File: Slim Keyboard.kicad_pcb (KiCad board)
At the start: 2 copper layers, 26 x 44 mm, 58 parts, among them J1 USB_C_Receptacle_USB2.0_16P, J2 SWD, J3 SWC, J5 S2B-PH-SM4-TB, U1 NRF52840-QIAA-R, U2 BQ24075RGT, U3 XC6220B331MR, Y1 ECS-.327-9-34B-TR, Y2 XRCGB32M000F1S2KR0

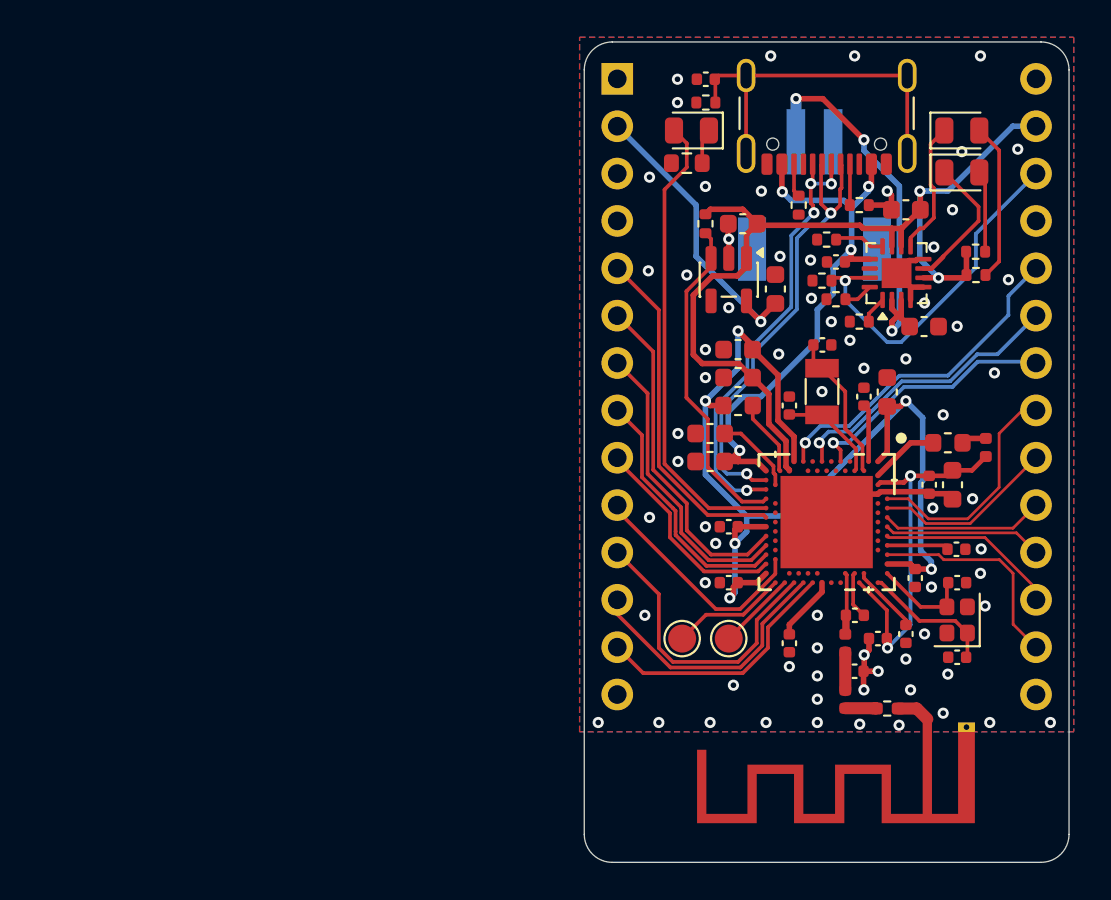
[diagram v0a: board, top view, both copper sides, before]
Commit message: DFM problems to solve; CE compliance issue
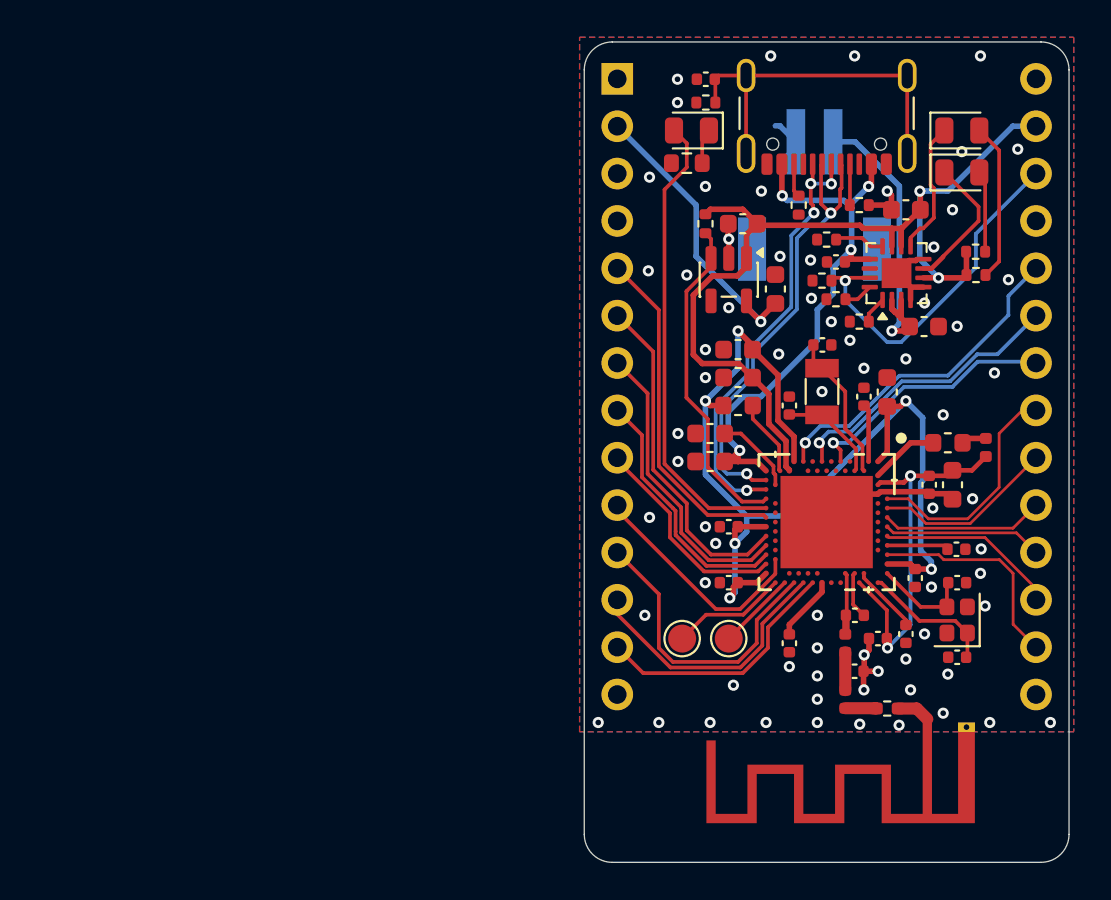
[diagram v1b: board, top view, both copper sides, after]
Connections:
- J5 pad 1: GND -> VBAT
- J5 pad 2: VBAT -> GND
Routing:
- net VBAT: track 21.9 -> 16.9 mm, vias 3 -> 1
- net GND: track 22.1 -> 25.1 mm
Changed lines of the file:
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@@
 		)
 		(pad "1" smd rect
-			(at 14.65 1.97 180)
+			(at 14.15 2.47 180)
 			(size 0.5 3.94)
 			(layers "F.Cu")
@@
 			(size 1 3.5)
 			(layers "B.Cu" "B.Mask" "B.Paste")
-			(net 1 "GND")
+			(net 17 "VBAT")
 			(pinfunction "1")
 			(pintype "passive")
@@
 			(size 1 3.5)
 			(layers "B.Cu" "B.Mask" "B.Paste")
-			(net 17 "VBAT")
+			(net 1 "GND")
 			(pinfunction "2")
 			(pintype "passive")
@@
 	)
 	(segment
+		(start 81.35 45.65)
+		(end 80.5 46.5)
+		(width 0.3)
+		(layer "B.Cu")
+		(net 1)
+	)
+	(segment
+		(start 80.492716 44.5)
+		(end 80.25 44.5)
+		(width 0.3)
+		(layer "B.Cu")
+		(net 1)
+	)
+	(segment
+		(start 81.35 45.357284)
+		(end 81.35 45.65)
+		(width 0.3)
+		(layer "B.Cu")
+		(net 1)
+	)
+	(segment
+		(start 81.35 45.357284)
+		(end 80.492716 44.5)
+		(width 0.3)
+		(layer "B.Cu")
+		(net 1)
+	)
+	(segment
+		(start 81.357742 45.349542)
+		(end 81.35 45.357284)
+		(width 0.6)
+		(layer "B.Cu")
+		(net 1)
+	)
+	(segment
 		(start 79.025 56.5)
 		(end 79.025 56.275)
@@
 	)
 	(segment
-		(start 84 73.73)
-		(end 84.02 73.75)
-		(width 0.2)
-		(layer "F.Cu")
-		(net 13)
-	)
-	(segment
-		(start 84 73.77)
-		(end 84.02 73.75)
-		(width 0.2)
-		(layer "F.Cu")
-		(net 13)
-	)
-	(segment
 		(start 81 71.77)
 		(end 81 71.25)
@@
 	)
 	(segment
-		(start 80.6 46.555)
-		(end 80.6 48.011026)
-		(width 0.3)
-		(layer "F.Cu")
-		(net 15)
-	)
-	(segment
-		(start 80.6 48.011026)
-		(end 80.623263 48.034289)
-		(width 0.3)
-		(layer "F.Cu")
-		(net 15)
-	)
-	(segment
 		(start 84.307625 51.145593)
 		(end 84.307625 51.592375)
@@
 	)
 	(segment
+		(start 80.6 48.226737)
+		(end 80.623263 48.25)
+		(width 0.3)
+		(layer "F.Cu")
+		(net 15)
+	)
+	(segment
 		(start 79.75 63)
 		(end 79.25 62.5)
@@
 	)
 	(segment
+		(start 80.6 46.555)
+		(end 80.6 48.226737)
+		(width 0.3)
+		(layer "F.Cu")
+		(net 15)
+	)
+	(segment
 		(start 79.25 62.5)
 		(end 78.25 62.5)
@@
 	)
 	(via
-		(at 80.623263 48.034289)
+		(at 80.623263 48.25)
 		(size 0.6)
 		(drill 0.3)
@@
 	)
 	(segment
+		(start 84.2149 48.7851)
+		(end 83.9298 48.5)
+		(width 0.3)
+		(layer "B.Cu")
+		(net 15)
+	)
+	(segment
 		(start 84.3399 50.897834)
 		(end 84.3399 48.9101)
@@
 	)
 	(segment
-		(start 81.088974 48.5)
-		(end 80.623263 48.034289)
+		(start 85.25 47.75)
+		(end 84.2149 48.7851)
 		(width 0.3)
 		(layer "B.Cu")
@@
 	)
 	(segment
-		(start 83.9298 48.5)
-		(end 81.088974 48.5)
-		(width 0.3)
-		(layer "B.Cu")
-		(net 15)
-	)
-	(segment
 		(start 82.5 54.355947)
 		(end 83.349 53.506947)
@@
 	)
 	(segment
-		(start 85.25 48)
-		(end 84.3399 48.9101)
+		(start 83.9298 48.5)
+		(end 80.873263 48.5)
 		(width 0.3)
 		(layer "B.Cu")
@@
 	)
 	(segment
-		(start 84.3399 48.9101)
-		(end 83.9298 48.5)
+		(start 77.721971 61.288621)
+		(end 77.721971 59.828324)
 		(width 0.3)
 		(layer "B.Cu")
@@
 	)
 	(segment
-		(start 85.25 47.75)
-		(end 85.25 48)
+		(start 84.3399 48.9101)
+		(end 84.2149 48.7851)
 		(width 0.3)
 		(layer "B.Cu")
@@
 	)
 	(segment
-		(start 77.721971 61.288621)
-		(end 77.721971 59.828324)
+		(start 77.721971 59.828324)
+		(end 78.525148 59.025147)
 		(width 0.3)
 		(layer "B.Cu")
@@
 	)
 	(segment
-		(start 77.721971 59.828324)
-		(end 78.525148 59.025147)
+		(start 80.873263 48.5)
+		(end 80.623263 48.25)
 		(width 0.3)
 		(layer "B.Cu")
@@
 	)
 	(segment
-		(start 85 45.25)
-		(end 82.793096 43.043096)
+		(start 87 54.5)
+		(end 87 54.814411)
 		(width 0.3)
 		(layer "F.Cu")
@@
 	)
 	(segment
-		(start 82.793096 43.043096)
-		(end 81.357742 43.043096)
+		(start 86.5 55.5)
+		(end 87.214411 55.5)
 		(width 0.3)
 		(layer "F.Cu")
@@
 	)
 	(segment
-		(start 86.5 55.5)
-		(end 86.5 55)
+		(start 87.214411 55.5)
+		(end 87.45 55.264411)
 		(width 0.3)
 		(layer "F.Cu")
@@
 	)
 	(segment
+		(start 87 54.5)
+		(end 86.685589 54.5)
+		(width 0.3)
+		(layer "F.Cu")
+		(net 17)
+	)
+	(segment
 		(start 87 53.8375)
-		(end 87 54.814411)
+		(end 87 54.5)
 		(width 0.3)
 		(layer "F.Cu")
@@
 	)
 	(segment
-		(start 86.5 55)
-		(end 86.842795 54.657205)
+		(start 86.685589 54.5)
+		(end 86.5 54.314411)
 		(width 0.3)
 		(layer "F.Cu")
@@
 	)
 	(via
-		(at 85 45.25)
-		(size 0.6)
-		(drill 0.3)
-		(layers "F.Cu" "B.Cu")
-		(free yes)
-		(net 17)
-	)
-	(via
 		(at 86.5 55.5)
 		(size 0.6)
@@
 		(net 17)
 	)
-	(via
-		(at 81.357742 43.043096)
-		(size 0.6)
-		(drill 0.3)
-		(layers "F.Cu" "B.Cu")
-		(free yes)
-		(net 17)
-	)
-	(segment
-		(start 81.357742 43.043096)
-		(end 81.357742 45.349542)
-		(width 0.6)
-		(layer "B.Cu")
-		(net 17)
-	)
 	(segment
 		(start 86.901 47.730346)
-		(end 85 45.829346)
-		(width 0.3)
-		(layer "B.Cu")
-		(net 17)
-	)
-	(segment
-		(start 85 45.829346)
-		(end 85 45.25)
+		(end 84.527938 45.357284)
 		(width 0.3)
 		(layer "B.Cu")
@@
 	)
 	(segment
-		(start 81.35 43.050838)
-		(end 81.357742 43.043096)
+		(start 84.527938 45.357284)
+		(end 83.35 45.357284)
 		(width 0.3)
 		(layer "B.Cu")
@@
 	)
 	(segment
-		(start 81.357742 45.349542)
-		(end 81.35 45.357284)
-		(width 0.6)
-		(layer "B.Cu")
-		(net 17)
-	)
-	(segment
 		(start 78.7 53.8875)
 		(end 78.7 54.209945)
@@
 		(polygon
 			(pts
+				(xy 85.5 54.25) (xy 86.5 54.25) (xy 86.5 55.5) (xy 85.5 55.5)
+			)
+		)
+	)
+	(zone
+		(net 0)
+		(net_name "")
+		(layer "F.Cu")
+		(hatch edge 0.5)
+		(connect_pads
+			(clearance 0)
+		)
+		(min_thickness 0.25)
+		(filled_areas_thickness no)
+		(keepout
+			(tracks allowed)
+			(vias allowed)
+			(pads allowed)
+			(copperpour not_allowed)
+			(footprints allowed)
+		)
+		(placement
+			(enabled no)
+			(sheetname "/mcu/")
+		)
+		(fill
+			(thermal_gap 0.5)
+			(thermal_bridge_width 0.5)
+		)
+		(polygon
+			(pts
 				(xy 84.25 49) (xy 86 49) (xy 86 49.75) (xy 84.25 49.75)
 			)
@@
 		(polygon
 			(pts
+				(xy 76.5 45.5) (xy 75.25 45.5) (xy 75.25 44.25) (xy 76.5 44.25)
+			)
+		)
+	)
+	(zone
+		(net 0)
+		(net_name "")
+		(layer "F.Cu")
+		(hatch edge 0.5)
+		(connect_pads
+			(clearance 0)
+		)
+		(min_thickness 0.25)
+		(filled_areas_thickness no)
+		(keepout
+			(tracks allowed)
+			(vias allowed)
+			(pads allowed)
+			(copperpour not_allowed)
+			(footprints allowed)
+		)
+		(placement
+			(enabled no)
+			(sheetname "/mcu/")
+		)
+		(fill
+			(thermal_gap 0.5)
+			(thermal_bridge_width 0.5)
+		)
+		(polygon
+			(pts
 				(xy 82.986812 72.50979) (xy 83 69.25) (xy 86.25 69.25) (xy 86.236812 72.50979)
 			)
@@
 		(polygon
 			(pts
+				(xy 80.75 54.5) (xy 78.25 54.5) (xy 78.25 53.25) (xy 77 53.25) (xy 77 52.75) (xy 80.75 52.75)
+			)
+		)
+	)
+	(zone
+		(net 0)
+		(net_name "")
+		(layer "F.Cu")
+		(hatch edge 0.5)
+		(connect_pads
+			(clearance 0)
+		)
+		(min_thickness 0.25)
+		(filled_areas_thickness no)
+		(keepout
+			(tracks allowed)
+			(vias allowed)
+			(pads allowed)
+			(copperpour not_allowed)
+			(footprints allowed)
+		)
+		(placement
+			(enabled no)
+			(sheetname "/mcu/")
+		)
+		(fill
+			(thermal_gap 0.5)
+			(thermal_bridge_width 0.5)
+		)
+		(polygon
+			(pts
 				(xy 79.25 62) (xy 86.75 62) (xy 86.75 69.5) (xy 79.25 69.5)
 			)
 		)
+	)
+	(zone
+		(net 0)
+		(net_name "")
+		(layer "F.Cu")
+		(hatch edge 0.5)
+		(connect_pads
+			(clearance 0)
+		)
+		(min_thickness 0.25)
+		(filled_areas_thickness no)
+		(keepout
+			(tracks allowed)
+			(vias allowed)
+			(pads allowed)
+			(copperpour not_allowed)
+			(footprints allowed)
+		)
+		(placement
+			(enabled no)
+			(sheetname "/mcu/")
+		)
+		(fill
+			(thermal_gap 0.5)
+			(thermal_bridge_width 0.5)
+		)
+		(polygon
+			(pts
+				(xy 82.75 51) (xy 83.5 51) (xy 83.5 51.5) (xy 82.75 51.5)
+			)
+		)

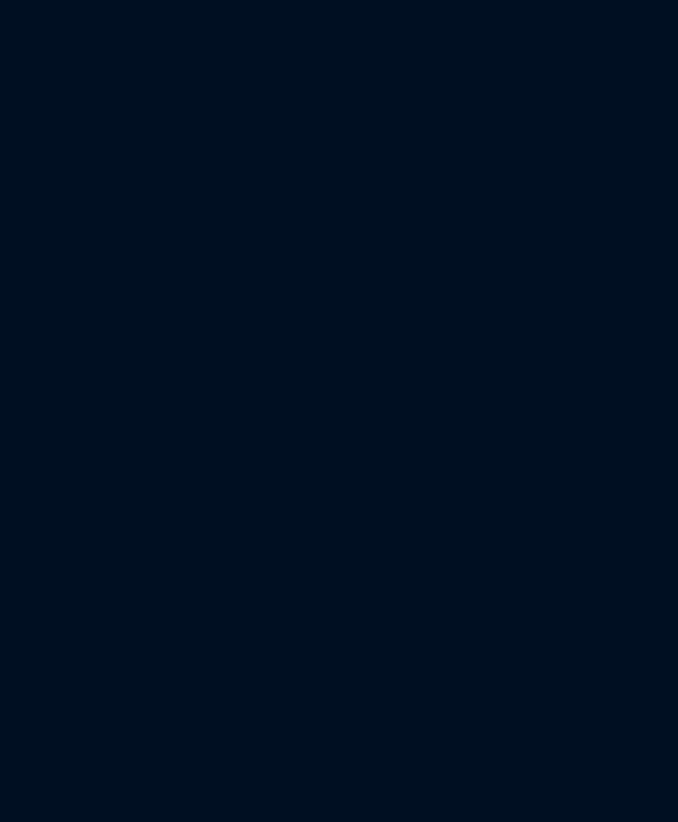
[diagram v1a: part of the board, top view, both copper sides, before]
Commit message: Replaced IC with NINA Module
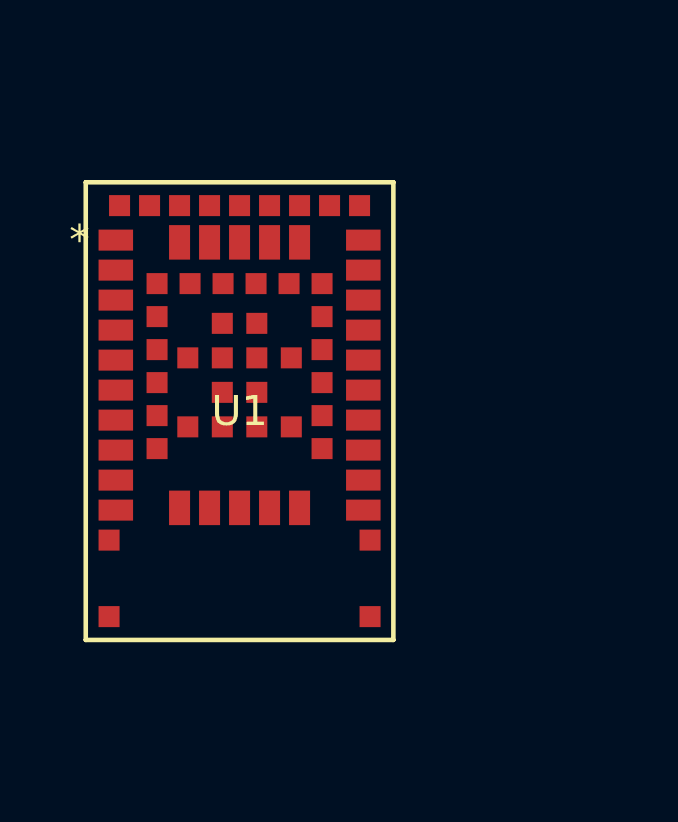
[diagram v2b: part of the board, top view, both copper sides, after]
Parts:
- added U1: NINA-B306-00B, NINA_B306_00B:NINA-B3x6_UBL, F.Cu at (46.6, 59.2)
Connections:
- J7 pad 10: PH5 -> D6
- J7 pad 11: PH6 -> D7
- J7 pad 12: PH7 -> D8
- J7 pad 13: PH8 -> D9
- J7 pad 14: unconnected-(J7-x-Pad14) -> D11
- J7 pad 15: unconnected-(J7-x-Pad15) -> D16
- J7 pad 16: PH9 -> D14
- J7 pad 17: PL10 -> D15
- J7 pad 18: PL11 -> D18
- J7 pad 19: PL12 -> D19
- J7 pad 2: EXT_VCC -> D1
- J7 pad 20: PL13 -> D20
- J7 pad 21: PL14 -> SYSOFF_SWITCH
- J7 pad 22: PL15 -> +3.3V
- J7 pad 23: PL16 -> RESET
- J7 pad 24: PL17 -> GND
- J7 pad 25: GND -> (no net)
- J7 pad 26: SYSOFF_SWITCH -> (no net)
- J7 pad 27: VDDH -> unconnected-(J7-BAT+-Pad27)
- J7 pad 28: GND -> unconnected-(J7-BAT+-Pad28)
- J7 pad 3: RESET -> D0
- J7 pad 5: PH0 -> GND
- J7 pad 6: PH1 -> D2
- J7 pad 7: PH2 -> D3
- J7 pad 8: PH3 -> D4
- J7 pad 9: PH4 -> D5
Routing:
- net RESET: vias 0 -> 1
- net PL17: vias 1 -> 0
- net PL16: vias 1 -> 0
- net PL15: vias 1 -> 0
- net GND: vias 69 -> 70
- net +3.3V: vias 0 -> 1
